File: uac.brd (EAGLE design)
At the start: 100 x 100 mm, 224 parts, among them Q1 2N7002CK4SST, Q2 2N7002CK4SST, Q3 2N7002CK4SST, Q4 2N7002CK4SST, Q5 2N7002CK4SST, U1 MCP73833-FCI/UN, U2 ADXL345, Y1 RESONATORSMD

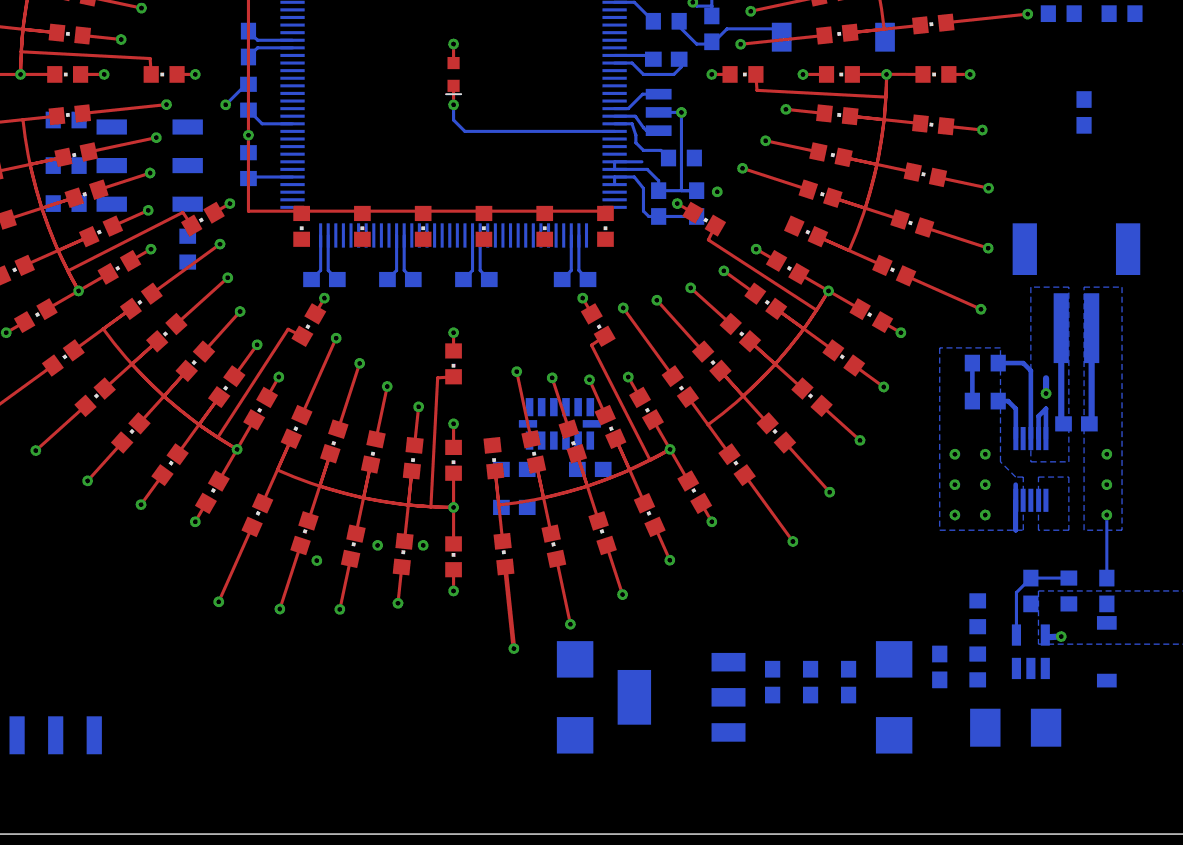
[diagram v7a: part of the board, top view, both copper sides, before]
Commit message: Debug serial port
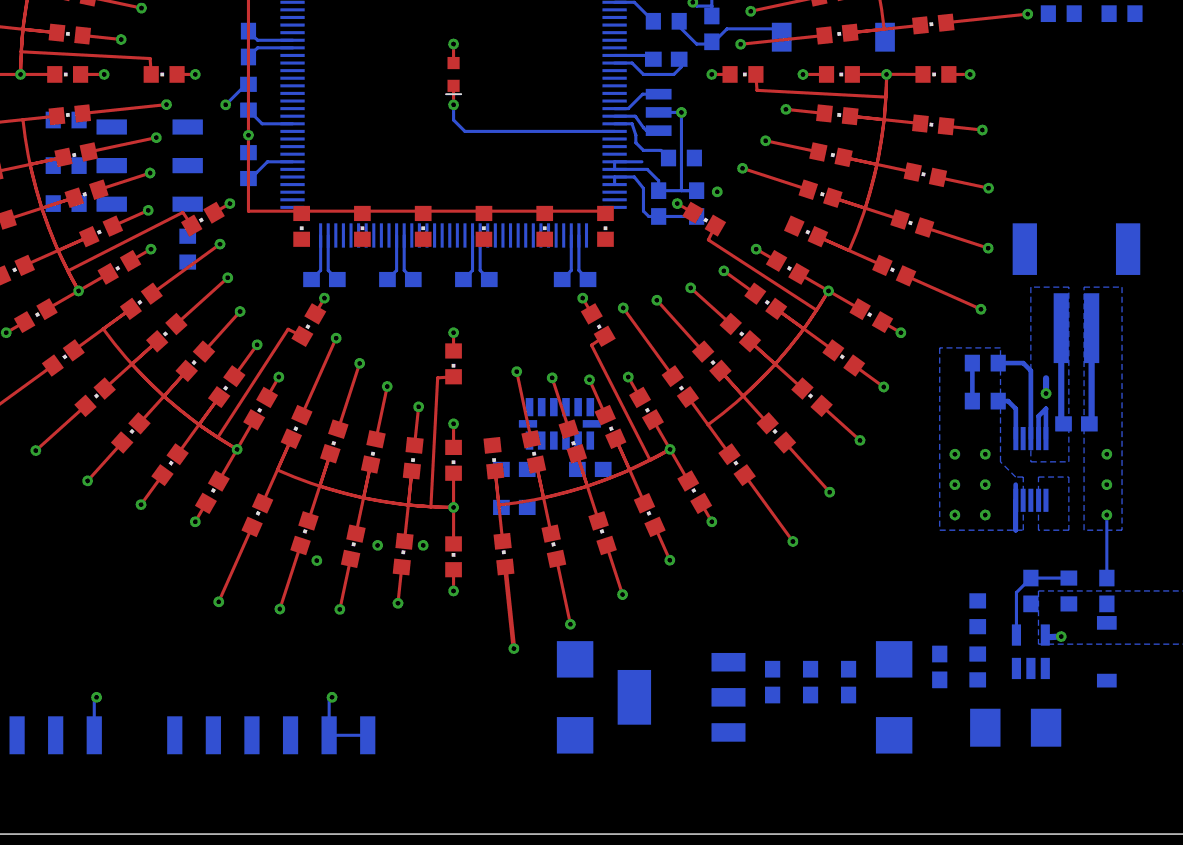
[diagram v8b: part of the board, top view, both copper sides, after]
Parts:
- removed C11: 100n, Custom components:C0603
- added FTDI: (no value), Custom components:1X06-SMD
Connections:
- removed net N$18: R12.2, U$1.77
- new net N$35: R12.2, U$1.79
- new net USART3_RX: FTDI.3, U$1.78
- new net USART3_TX: FTDI.2, U$1.77
- net +3V3: no longer C11.1
- net GND: now also FTDI.5, FTDI.6; no longer C11.2
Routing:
- net GND: track 78.6 -> 87.8 mm, vias 20 -> 22
- net N$35: track 0.00 -> 3.36 mm
- net N$18: track 2.94 -> 0.00 mm
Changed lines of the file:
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@@
 <element name="C9" library="Custom components" package="C0603" value="100n" x="36.5" y="52" rot="MR270"/>
 <element name="C10" library="Custom components" package="C0603" value="100n" x="36.5" y="58.5" rot="MR270"/>
-<element name="C11" library="Custom components" package="C0603" value="100n" x="91.5" y="47.5" rot="MR90"/>
 <element name="C12" library="Custom components" package="C0603" value="100n" x="64" y="51" rot="MR0"/>
 <element name="C13" library="Custom components" package="C0603" value="100n" x="58.5" y="63.5" rot="MR0"/>
@@
 </element>
 <element name="R27" library="Custom components" package="R0603" value="10k" x="36.5" y="48.5" rot="MR90"/>
+<element name="FTDI" library="Custom components" package="1X06-SMD" value="" x="38" y="10" rot="MR0"/>
 </elements>
 <signals>
@@
 <contactref element="C13" pad="2"/>
 <contactref element="C12" pad="2"/>
-<contactref element="C11" pad="2"/>
 <contactref element="C10" pad="2"/>
 <contactref element="C9" pad="2"/>
@@
 <via x="50" y="52" extent="1-16" drill="0.31"/>
 <wire x1="50" y1="52" x2="49" y2="52" width="0.2032" layer="2"/>
-<wire x1="92" y1="33.3" x2="91.5" y2="48.35" width="0" layer="19" extent="16-16"/>
+<contactref element="FTDI" pad="5"/>
+<contactref element="FTDI" pad="6"/>
+<wire x1="26.35" y1="6.5" x2="26.35" y2="8.85" width="0.2032" layer="16"/>
+<wire x1="26.35" y1="8.85" x2="26.5" y2="9" width="0.2032" layer="16"/>
+<via x="26.5" y="9" extent="1-16" drill="0.31"/>
+<wire x1="26.5" y1="9" x2="27" y2="9" width="0.2032" layer="2"/>
+<wire x1="41.81" y1="6.5" x2="44.35" y2="6.5" width="0.2032" layer="16"/>
+<wire x1="41.81" y1="6.5" x2="41.81" y2="8.81" width="0.2032" layer="16"/>
+<wire x1="41.81" y1="8.81" x2="42" y2="9" width="0.2032" layer="16"/>
+<via x="42" y="9" extent="1-16" drill="0.31"/>
+<wire x1="42" y1="9" x2="43" y2="9" width="0.2032" layer="2"/>
+<wire x1="55.75" y1="60.6" x2="58.25" y2="60.6" width="0" layer="19" extent="16-16"/>
+<wire x1="51.75" y1="60.6" x2="55.75" y2="60.6" width="0" layer="19" extent="16-16"/>
+<wire x1="46.75" y1="62.9" x2="51.15" y2="63.5" width="0" layer="19" extent="16-16"/>
+<wire x1="39.4" y1="58.25" x2="46.75" y2="60.6" width="0" layer="19" extent="16-16"/>
+<wire x1="37.1" y1="51.75" x2="36.5" y2="57.65" width="0" layer="19" extent="16-16"/>
+<wire x1="39.4" y1="46.25" x2="39.4" y2="51.75" width="0" layer="19" extent="16-16"/>
+<wire x1="41.75" y1="39.4" x2="39.4" y2="46.25" width="0" layer="19" extent="16-16"/>
+<wire x1="46.75" y1="37.1" x2="42.35" y2="36.5" width="0" layer="19" extent="16-16"/>
+<wire x1="51.75" y1="37.1" x2="47.35" y2="36.5" width="0" layer="19" extent="16-16"/>
+<wire x1="58.25" y1="37.1" x2="52.35" y2="36.5" width="0" layer="19" extent="16-16"/>
+<wire x1="60.6" y1="43.75" x2="58.25" y2="39.4" width="0" layer="19" extent="16-16"/>
 <wire x1="63.15" y1="51" x2="63.5" y2="47.5" width="0" layer="19" extent="16-16"/>
 <wire x1="88" y1="15.15" x2="87.0094" y2="20.0094" width="0" layer="19" extent="16-16"/>
 <wire x1="84.5" y1="15.35" x2="88" y2="15.15" width="0" layer="19" extent="16-16"/>
 <wire x1="88" y1="10.9" x2="88" y2="15.15" width="0" layer="19" extent="16-16"/>
-<wire x1="58.25" y1="39.4" x2="60.6" y2="43.75" width="0" layer="19" extent="16-16"/>
-<wire x1="52.35" y1="36.5" x2="58.25" y2="37.1" width="0" layer="19" extent="16-16"/>
-<wire x1="47.35" y1="36.5" x2="51.75" y2="37.1" width="0" layer="19" extent="16-16"/>
-<wire x1="42.35" y1="36.5" x2="46.75" y2="37.1" width="0" layer="19" extent="16-16"/>
 <wire x1="79" y1="11.5" x2="84.5" y2="15.35" width="0" layer="19" extent="16-16"/>
 <wire x1="76" y1="10.85" x2="79" y2="11.5" width="0" layer="19" extent="16-16"/>
@@
 <wire x1="71" y1="10.85" x2="73.5" y2="10.85" width="0" layer="19" extent="16-16"/>
 <wire x1="68.0988" y1="11.3114" x2="71" y2="10.85" width="0" layer="19" extent="16-16"/>
-<wire x1="39.4" y1="46.25" x2="41.75" y2="39.4" width="0" layer="19" extent="16-16"/>
-<wire x1="39.4" y1="51.75" x2="39.4" y2="46.25" width="0" layer="19" extent="16-16"/>
-<wire x1="36.5" y1="57.65" x2="37.1" y2="51.75" width="0" layer="19" extent="16-16"/>
 <wire x1="32.5" y1="44" x2="39.4" y2="46.25" width="0" layer="19" extent="16-16"/>
 <wire x1="54.85" y1="21.5" x2="48" y2="19" width="0" layer="19" extent="16-16"/>
@@
 <wire x1="58.2" y1="25.9" x2="56.6" y2="25.9" width="0" layer="19" extent="16-16"/>
 <wire x1="58.15" y1="24" x2="58.2" y2="25.9" width="0" layer="19" extent="16-16"/>
-<wire x1="46.75" y1="60.6" x2="39.4" y2="58.25" width="0" layer="19" extent="16-16"/>
-<wire x1="51.15" y1="63.5" x2="46.75" y2="62.9" width="0" layer="19" extent="16-16"/>
-<wire x1="55.75" y1="60.6" x2="51.75" y2="60.6" width="0" layer="19" extent="16-16"/>
-<wire x1="58.25" y1="60.6" x2="55.75" y2="60.6" width="0" layer="19" extent="16-16"/>
 <wire x1="58" y1="6.5" x2="68.0988" y2="11.3114" width="0" layer="19" extent="16-16"/>
-<wire x1="26.35" y1="6.5" x2="41" y2="18" width="0" layer="19" extent="16-16"/>
 </signal>
 <signal name="+3V3">
@@
 <contactref element="C9" pad="1"/>
 <contactref element="C10" pad="1"/>
-<contactref element="C11" pad="1"/>
 <contactref element="C12" pad="1"/>
 <contactref element="C13" pad="1"/>
@@
 <contactref element="U$9" pad="3"/>
 <contactref element="R27" pad="1"/>
-<wire x1="65.85" y1="44.5" x2="91.5" y2="46.65" width="0" layer="19" extent="16-16"/>
+<wire x1="39.4" y1="46.75" x2="37.4" y2="46.75" width="0.2032" layer="16"/>
+<wire x1="37.4" y1="46.75" x2="36.5" y2="47.65" width="0.2032" layer="16"/>
+<wire x1="60.6" y1="56.25" x2="58.75" y2="60.6" width="0" layer="19" extent="16-16"/>
+<wire x1="60.6" y1="50.75" x2="60.6" y2="56.25" width="0" layer="19" extent="16-16"/>
+<wire x1="65.85" y1="44.5" x2="64.5" y2="50" width="0" layer="19" extent="16-16"/>
 <wire x1="66" y1="40.65" x2="65.85" y2="44.5" width="0" layer="19" extent="16-16"/>
 <wire x1="57.75" y1="39.4" x2="60.6" y2="42.75" width="0" layer="19" extent="16-16"/>
-<wire x1="64.5" y1="50" x2="65.85" y2="44.5" width="0" layer="19" extent="16-16"/>
-<wire x1="60.6" y1="56.25" x2="60.6" y2="50.75" width="0" layer="19" extent="16-16"/>
-<wire x1="58.75" y1="60.6" x2="60.6" y2="56.25" width="0" layer="19" extent="16-16"/>
 <wire x1="52.85" y1="63.5" x2="58.75" y2="62.9" width="0" layer="19" extent="16-16"/>
 <wire x1="47.85" y1="63.5" x2="52.25" y2="62.9" width="0" layer="19" extent="16-16"/>
@@
 <wire x1="71" y1="9.15" x2="68.0988" y2="9" width="0" layer="19" extent="16-16"/>
 <wire x1="21.27" y1="6.5" x2="32.5" y2="37.65" width="0" layer="19" extent="16-16"/>
-<wire x1="39.4" y1="46.75" x2="37.4" y2="46.75" width="0.2032" layer="16"/>
-<wire x1="37.4" y1="46.75" x2="36.5" y2="47.65" width="0.2032" layer="16"/>
 </signal>
 <signal name="N$1">
@@
 <wire x1="60.6" y1="48.25" x2="89.15" y2="54" width="0" layer="19" extent="16-16"/>
 </signal>
-<signal name="N$18">
-<contactref element="R12" pad="2"/>
-<contactref element="U$1" pad="77"/>
-<wire x1="39.4" y1="43.25" x2="36.6" y2="43.25" width="0.2032" layer="16"/>
-<wire x1="36.6" y1="43.25" x2="36.5" y2="43.15" width="0.2032" layer="16"/>
-</signal>
 <signal name="STAT2">
 <contactref element="U1" pad="4"/>
@@
 <wire x1="11.11" y1="6.5" x2="42.25" y2="39.4" width="0" layer="19" extent="16-16"/>
 </signal>
+<signal name="USART3_TX">
+<contactref element="U$1" pad="77"/>
+<contactref element="FTDI" pad="2"/>
+<wire x1="34.19" y1="6.5" x2="39.4" y2="43.25" width="0" layer="19" extent="16-16"/>
+</signal>
+<signal name="USART3_RX">
+<contactref element="U$1" pad="78"/>
+<contactref element="FTDI" pad="3"/>
+<wire x1="36.73" y1="6.5" x2="39.4" y2="43.75" width="0" layer="19" extent="16-16"/>
+</signal>
+<signal name="N$35">
+<contactref element="U$1" pad="79"/>
+<contactref element="R12" pad="2"/>
+<wire x1="39.4" y1="44.25" x2="37.75" y2="44.25" width="0.2032" layer="16"/>
+<wire x1="37.75" y1="44.25" x2="37" y2="43.5" width="0.2032" layer="16"/>
+<wire x1="37" y1="43.5" x2="36.85" y2="43.5" width="0.2032" layer="16"/>
+<wire x1="36.85" y1="43.5" x2="36.5" y2="43.15" width="0.2032" layer="16"/>
+</signal>
 </signals>
